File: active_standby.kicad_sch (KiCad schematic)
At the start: 13 parts, among them Q2 BSS138, U24 SN3257QDYYRQ1, U30 SN3257QDYYRQ1

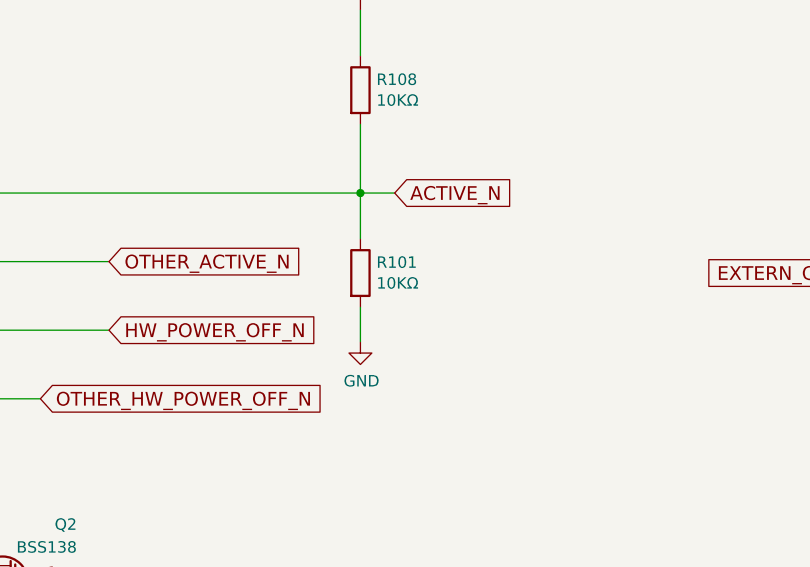
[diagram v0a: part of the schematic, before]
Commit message: Update schematics to match what is done to the boards so far
Get ready to split off a branch where the updates to the board can be
done while still keeping updates for the prototypes.

Signed-off-by: Corey Minyard <corey@minyard.net>
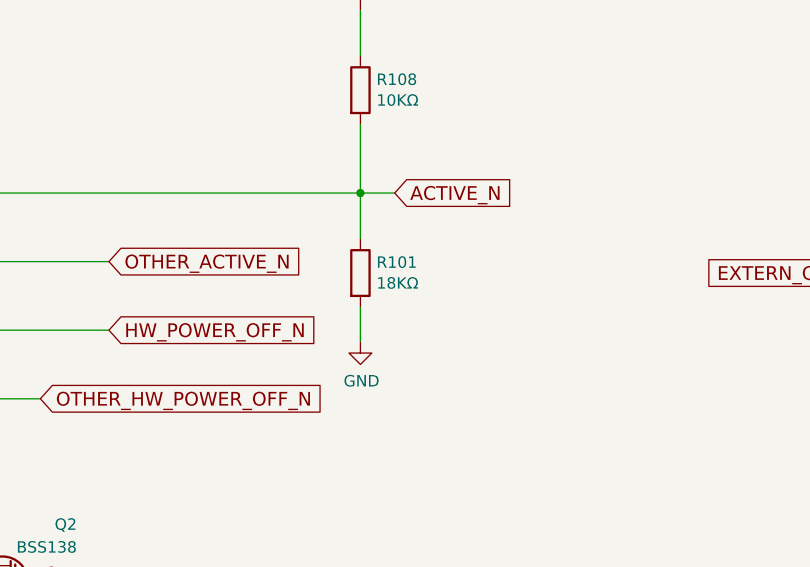
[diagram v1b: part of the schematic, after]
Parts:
- R101: value 10KΩ -> 18KΩ
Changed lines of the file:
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@@
 			)
 		)
-		(property "Value" "10KΩ"
+		(property "Value" "18KΩ"
 			(at 173.228 135.763 0)
 			(effects

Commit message: Get rid of the resistor on OTHER_PRESENCE_N
You can just use the pullup on the GPIO pin.

Signed-off-by: Corey Minyard <corey@minyard.net>
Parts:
- removed R102: 1MΩ, Resistor_SMD:R_0402_1005Metric_Pad0.72x0.64mm_HandSolder, symbol Device:R
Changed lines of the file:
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@@
-	)
-	(junction
-		(at 134.62 69.85)
-		(diameter 0)
-		(color 0 0 0 0)
 	)
 	(junction
@@
 	(wire
 		(pts
-			(xy 134.62 69.85) (xy 142.24 69.85)
-		)
-		(stroke
-			(width 0)
-			(type default)
-		)
-	)
-	(wire
-		(pts
 			(xy 92.71 173.99) (xy 124.46 173.99)
 		)
@@
 	(wire
 		(pts
-			(xy 134.62 36.83) (xy 134.62 69.85)
-		)
-		(stroke
-			(width 0)
-			(type default)
-		)
-	)
-	(wire
-		(pts
 			(xy 59.69 41.91) (xy 68.58 41.91)
 		)
@@
 	(wire
 		(pts
-			(xy 109.22 69.85) (xy 134.62 69.85)
+			(xy 109.22 69.85) (xy 142.24 69.85)
 		)
 		(stroke
@@
 		(pts
 			(xy 69.85 135.89) (xy 62.23 135.89)
-		)
-		(stroke
-			(width 0)
-			(type default)
-		)
-	)
-	(wire
-		(pts
-			(xy 134.62 25.4) (xy 134.62 29.21)
 		)
 		(stroke
@@
 	)
 	(symbol
-		(lib_id "power:+3.3V")
-		(at 134.62 25.4 0)
-		(unit 1)
-		(exclude_from_sim no)
-		(in_bom yes)
-		(on_board yes)
-		(dnp no)
-		(fields_autoplaced yes)
-		(property "Reference" "#PWR0266"
-			(at 134.62 29.21 0)
-			(effects
-				(font
-					(size 1.27 1.27)
-				)
-				(hide yes)
-			)
-		)
-		(property "Value" "+3.3V"
-			(at 134.62 21.59 0)
-			(effects
-				(font
-					(size 1.27 1.27)
-				)
-			)
-		)
-		(property "Footprint" ""
-			(at 134.62 25.4 0)
-			(effects
-				(font
-					(size 1.27 1.27)
-				)
-				(hide yes)
-			)
-		)
-		(property "Datasheet" ""
-			(at 134.62 25.4 0)
-			(effects
-				(font
-					(size 1.27 1.27)
-				)
-				(hide yes)
-			)
-		)
-		(property "Description" ""
-			(at 134.62 25.4 0)
-			(effects
-				(font
-					(size 1.27 1.27)
-				)
-			)
-		)
-		(pin "1"
-		)
-		(instances
-			(project "PacSat_AFSK"
-				(path "/cc9f42d2-6985-41ac-acab-5ab7b01c5b38/4fa888af-703c-49ed-93bb-d56d2f02c470"
-					(reference "#PWR0266")
-					(unit 1)
-				)
-			)
-		)
-	)
-	(symbol
 		(lib_id "Device:R")
 		(at 238.76 142.24 0)
@@
 					(unit 1)
 				)
-			)
-		)
-	)
-	(symbol
-		(lib_id "Device:R")
-		(at 134.62 33.02 0)
-		(unit 1)
-		(exclude_from_sim no)
-		(in_bom yes)
-		(on_board yes)
-		(dnp no)
-		(property "Reference" "R102"
-			(at 136.398 31.8516 0)
-			(effects
-				(font
-					(size 1.27 1.27)
-				)
-				(justify left)
-			)
-		)
-		(property "Value" "1MΩ"
-			(at 136.398 34.163 0)
-			(effects
-				(font
-					(size 1.27 1.27)
-				)
-				(justify left)
-			)
-		)
-		(property "Footprint" "Resistor_SMD:R_0402_1005Metric_Pad0.72x0.64mm_HandSolder"
-			(at 132.842 33.02 90)
-			(effects
-				(font
-					(size 1.27 1.27)
-				)
-				(hide yes)
-			)
-		)
-		(property "Datasheet" "~"
-			(at 134.62 33.02 0)
-			(effects
-				(font
-					(size 1.27 1.27)
-				)
-				(hide yes)
-			)
-		)
-		(property "Description" ""
-			(at 134.62 33.02 0)
-			(effects
-				(font
-					(size 1.27 1.27)
-				)
-			)
-		)
-		(pin "1"
-		)
-		(pin "2"
-		)
-		(instances
-			(project "PacSat_AFSK"
-				(path "/cc9f42d2-6985-41ac-acab-5ab7b01c5b38/4fa888af-703c-49ed-93bb-d56d2f02c470"
-					(reference "R102")
-					(unit 1)
-				)

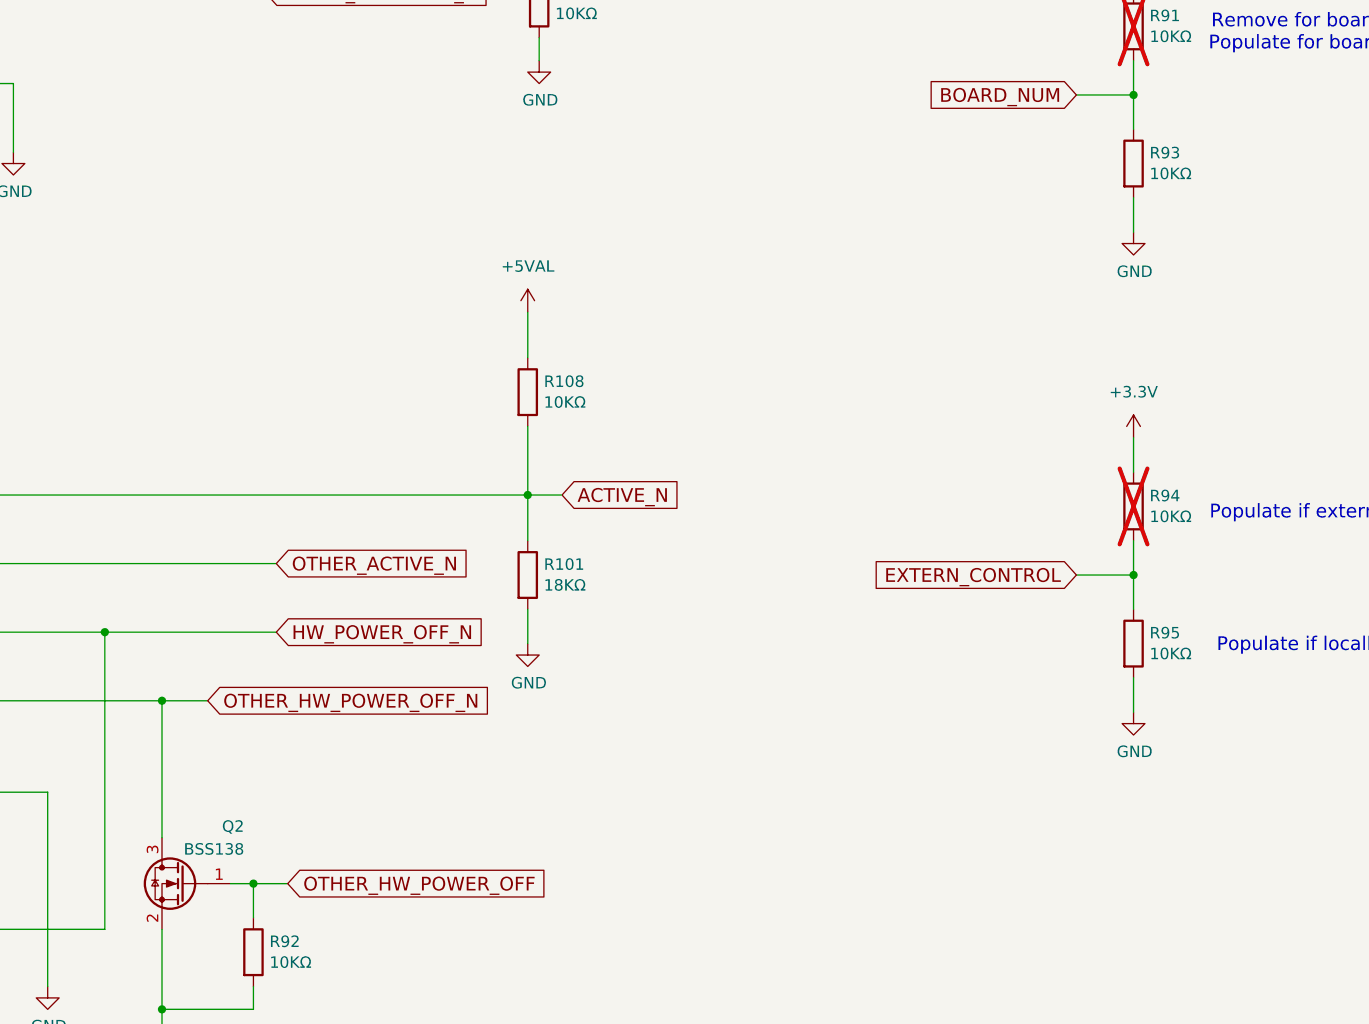
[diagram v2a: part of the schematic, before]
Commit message: Pull 0 ohm power supply resistors away from connector
It's really hard to solder them otherwise.

Also change the BOARD_NUM pulldown resistor to 18K so the value
is close to 3V when the pullup is installed.

Signed-off-by: Corey Minyard <corey@minyard.net>
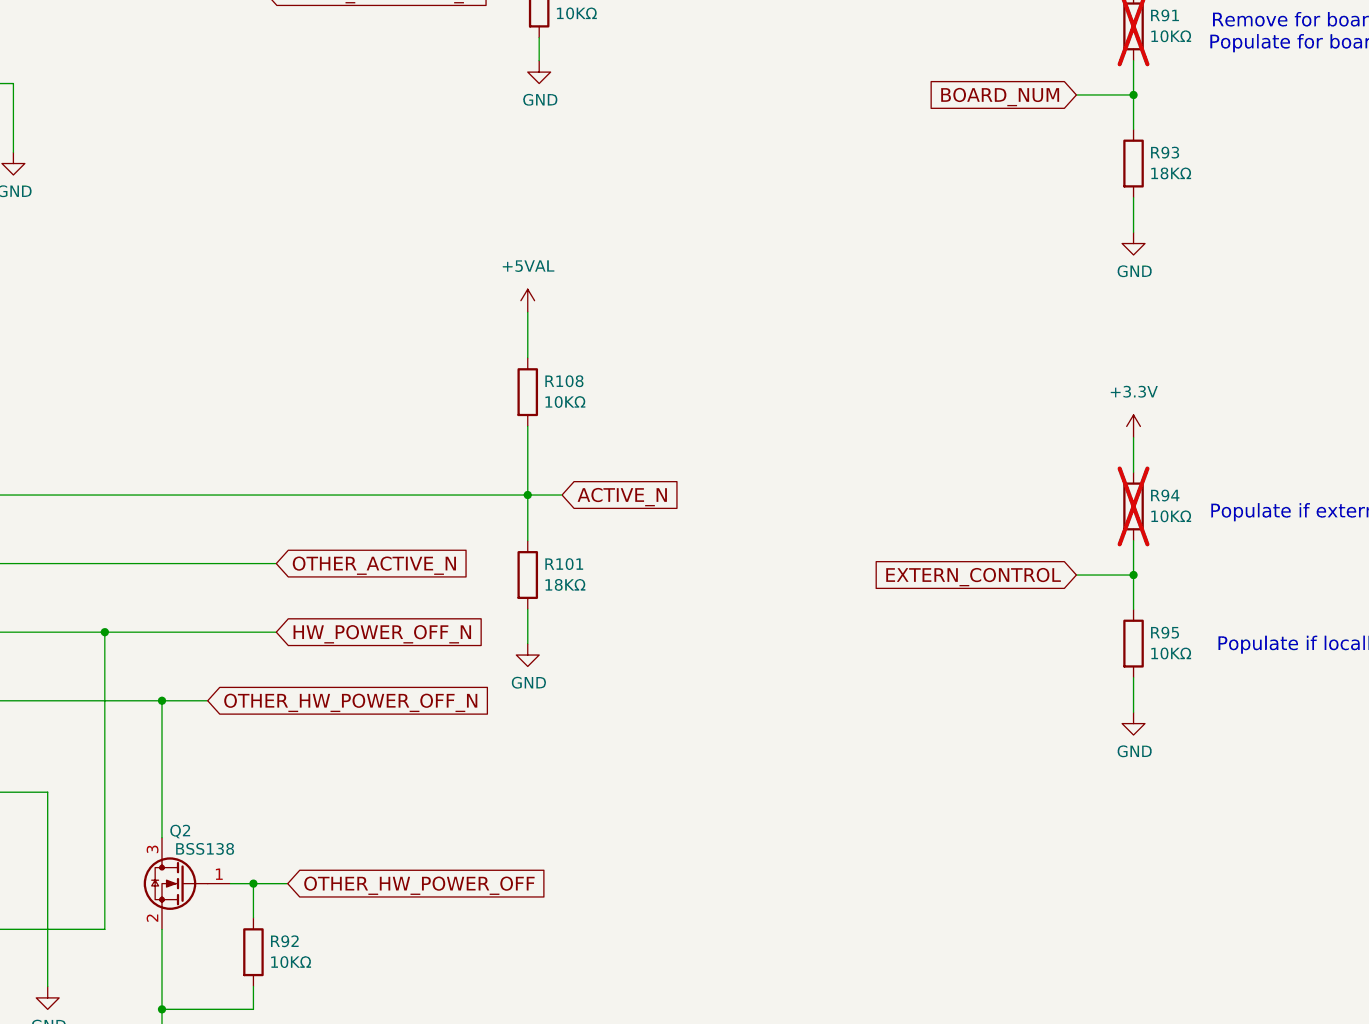
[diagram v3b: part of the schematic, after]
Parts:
- R93: value 10KΩ -> 18KΩ
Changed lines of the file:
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@@
 		(dnp no)
 		(property "Reference" "Q2"
-			(at 139.954 162.56 0)
+			(at 134.112 163.068 0)
 			(effects
 				(font
@@
 		)
 		(property "Value" "BSS138"
-			(at 139.954 165.1 0)
+			(at 138.938 165.1 0)
 			(effects
 				(font
@@
 			)
 		)
-		(property "Value" "10KΩ"
+		(property "Value" "18KΩ"
 			(at 240.538 90.043 0)
 			(effects

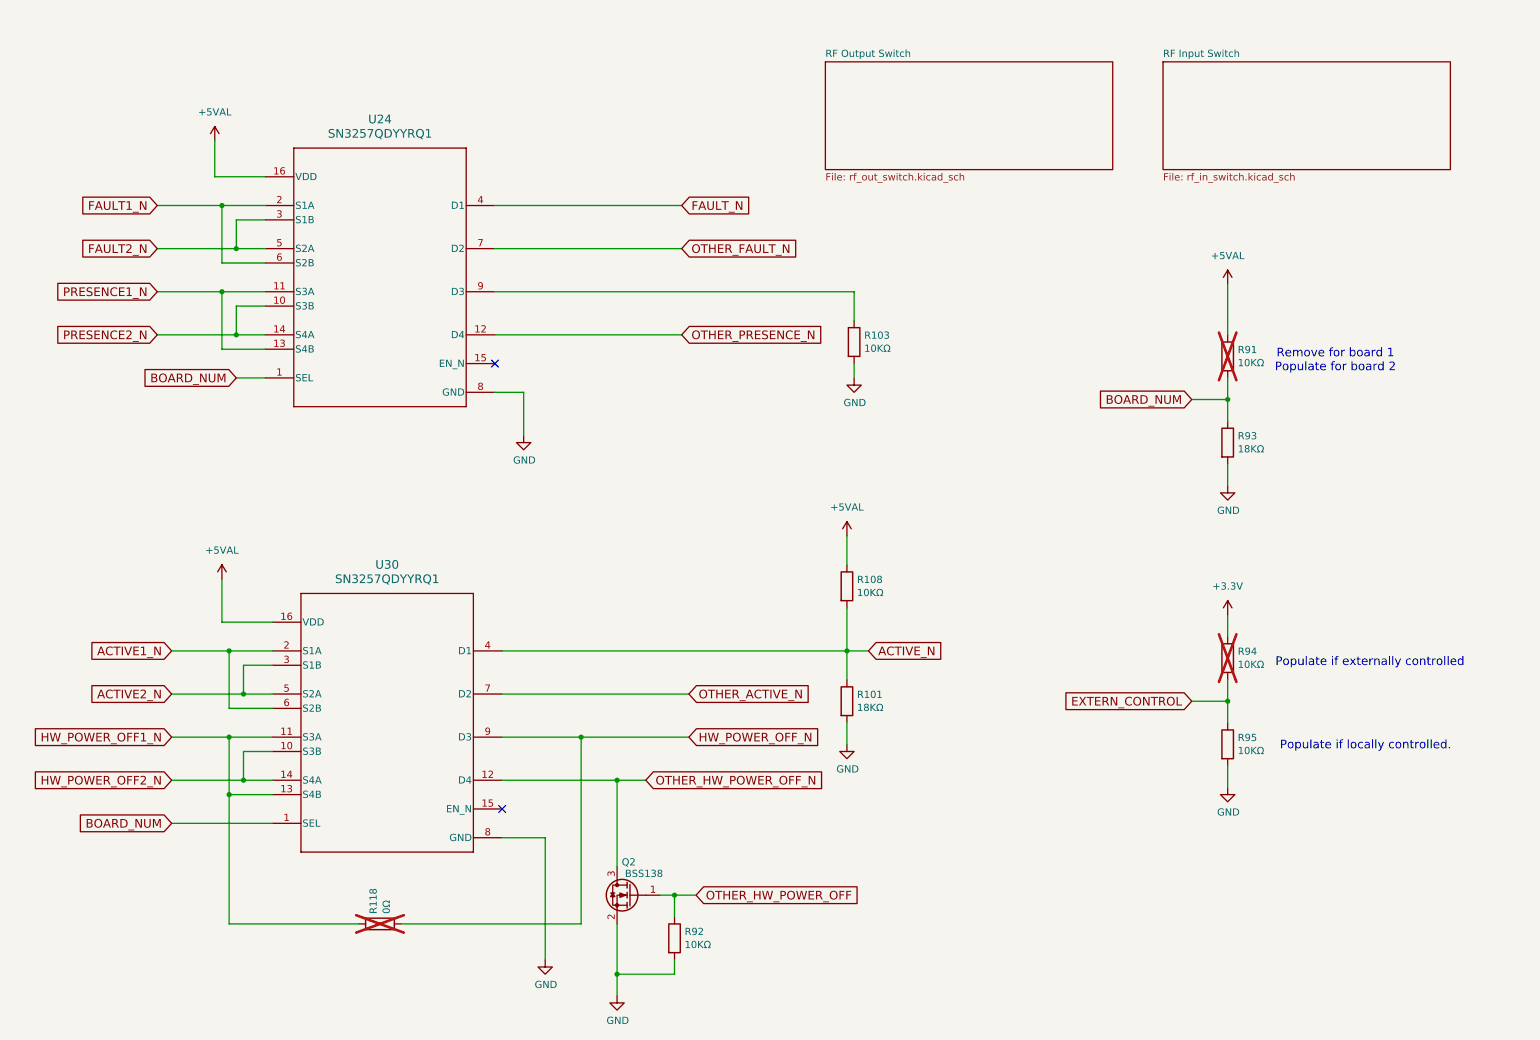
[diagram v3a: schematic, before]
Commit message: Add a buffer from OTHER_HW_POWER_OFF_N to the CPU
That particular line is also hooked to the power disable on the other
board.  If you reset the other board, when the other board is powered
off, the CPU appears to pull the OTHER_HW_POWER_OFF_N down pretty
strongly causing a reset on the first board.

Add a buffer going into the CPU to fix the issue.

Signed-off-by: Corey Minyard <corey@minyard.net>
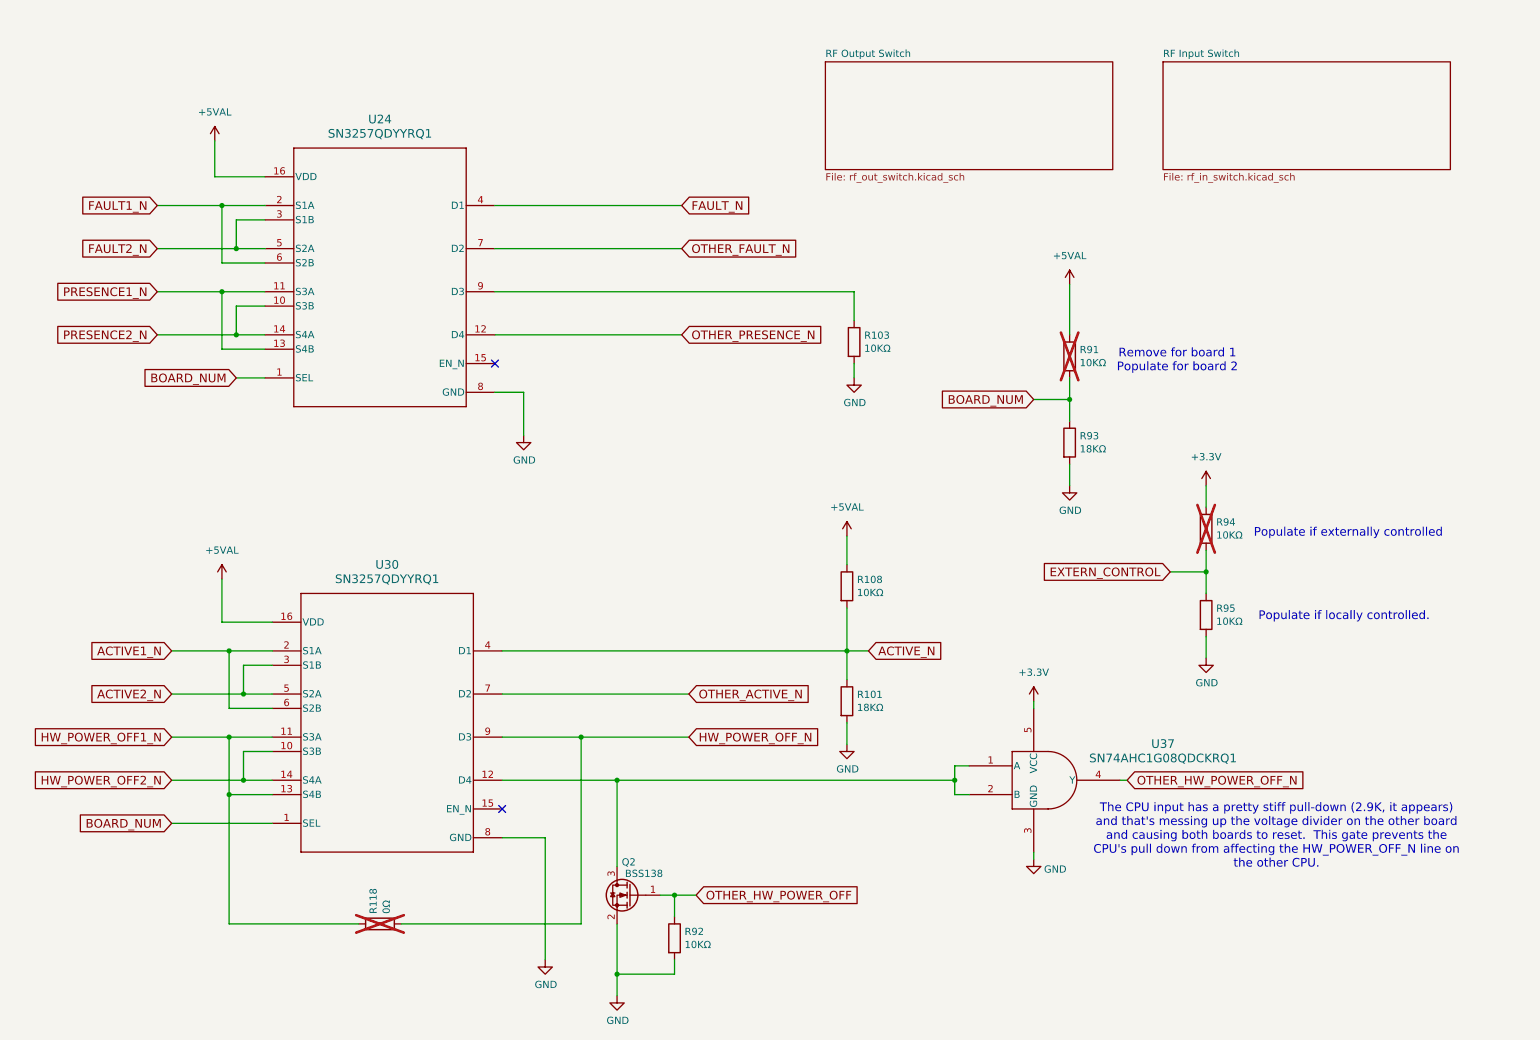
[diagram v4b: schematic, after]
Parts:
- added U37: SN74AHC1G08QDCKRQ1, PacSatDev_ti:DCK5, symbol PACSAT_ICs:SN74AHC1G08QDCKRQ1
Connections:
- net +3.3V: now also U37.5 (VCC)
- net GND: now also U37.3 (GND)
- net OTHER_HW_POWER_OFF_N: now also U37.4 (Y); no longer Q2.3 (D), U30.12 (D4)
- new net: Q2.3 (D), U30.12 (D4), U37.1 (A), U37.2 (B)
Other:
- note added: "The CPU input has a pretty stiff pull-down (2.9K, it appears) and that's messing up the voltage divider on the other board and causing both boards to reset. This gate prevents the CPU's pull down from affecting the HW_POWER_OFF_N line on the other CPU."
- moved on the sheet: R91, R93, R94, R95
